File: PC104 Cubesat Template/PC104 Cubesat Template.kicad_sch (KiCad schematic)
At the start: 10 parts

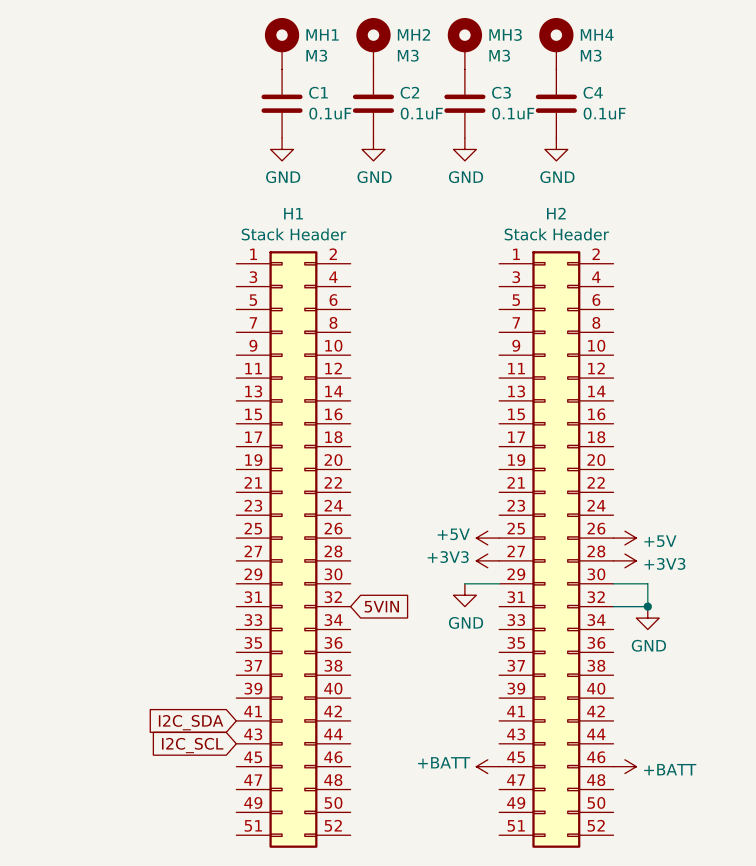
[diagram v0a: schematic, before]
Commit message: add tj bus specific pins
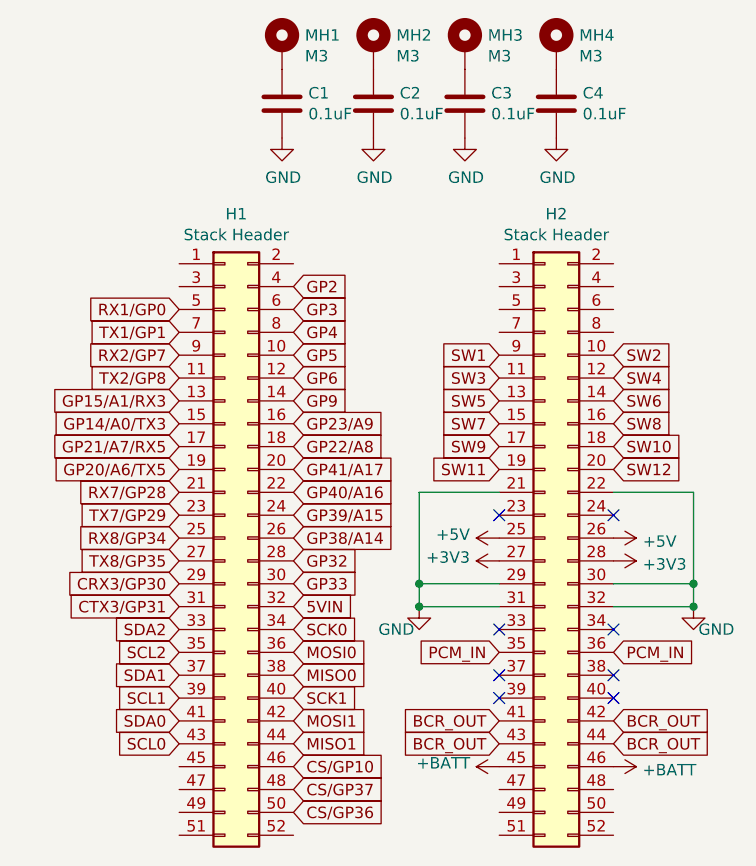
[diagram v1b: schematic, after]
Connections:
- net GND: now also H2.21 (Pin_21), H2.22 (Pin_22), H2.31 (Pin_31)
- net GP5: now reaches H1.10 (Pin_10)
- net TX2/GP8: now reaches H1.11 (Pin_11)
- net GP6: now reaches H1.12 (Pin_12)
- net GP15/A1/RX3: now reaches H1.13 (Pin_13)
- net GP9: now reaches H1.14 (Pin_14)
- net GP14/A0/TX3: now reaches H1.15 (Pin_15)
- net GP23/A9: now reaches H1.16 (Pin_16)
- net GP21/A7/RX5: now reaches H1.17 (Pin_17)
- net GP22/A8: now reaches H1.18 (Pin_18)
- net GP20/A6/TX5: now reaches H1.19 (Pin_19)
- net GP41/A17: now reaches H1.20 (Pin_20)
- net RX7/GP28: now reaches H1.21 (Pin_21)
- net GP40/A16: now reaches H1.22 (Pin_22)
- net TX7/GP29: now reaches H1.23 (Pin_23)
- net GP39/A15: now reaches H1.24 (Pin_24)
- net RX8/GP34: now reaches H1.25 (Pin_25)
- net GP38/A14: now reaches H1.26 (Pin_26)
- net TX8/GP35: now reaches H1.27 (Pin_27)
- net GP32: now reaches H1.28 (Pin_28)
- net CRX3/GP30: now reaches H1.29 (Pin_29)
- net GP33: now reaches H1.30 (Pin_30)
- net CTX3/GP31: now reaches H1.31 (Pin_31)
- net SDA2: now reaches H1.33 (Pin_33)
- net SCK0: now reaches H1.34 (Pin_34)
- net SCL2: now reaches H1.35 (Pin_35)
- net MOSI0: now reaches H1.36 (Pin_36)
- net SDA1: now reaches H1.37 (Pin_37)
- net MISO0: now reaches H1.38 (Pin_38)
- net SCL1: now reaches H1.39 (Pin_39)
- net GP2: now reaches H1.4 (Pin_4)
- net SCK1: now reaches H1.40 (Pin_40)
- net MOSI1: now reaches H1.42 (Pin_42)
- net MISO1: now reaches H1.44 (Pin_44)
- net CS/GP10: now reaches H1.46 (Pin_46)
- net CS/GP37: now reaches H1.48 (Pin_48)
- net RX1/GP0: now reaches H1.5 (Pin_5)
- net CS/GP36: now reaches H1.50 (Pin_50)
- net GP3: now reaches H1.6 (Pin_6)
- net TX1/GP1: now reaches H1.7 (Pin_7)
- net GP4: now reaches H1.8 (Pin_8)
- net RX2/GP7: now reaches H1.9 (Pin_9)
- net SW2: now reaches H2.10 (Pin_10)
- net SW3: now reaches H2.11 (Pin_11)
- net SW4: now reaches H2.12 (Pin_12)
- net SW5: now reaches H2.13 (Pin_13)
- net SW6: now reaches H2.14 (Pin_14)
- net SW7: now reaches H2.15 (Pin_15)
- net SW8: now reaches H2.16 (Pin_16)
- net SW9: now reaches H2.17 (Pin_17)
- net SW10: now reaches H2.18 (Pin_18)
- net SW11: now reaches H2.19 (Pin_19)
- net SW12: now reaches H2.20 (Pin_20)
- net PCM_IN: now reaches H2.35 (Pin_35)
- net PCM_IN: now also H2.36 (Pin_36)
- net BCR_OUT: now reaches H2.41 (Pin_41)
- net BCR_OUT: now also H2.42 (Pin_42), H2.43 (Pin_43), H2.44 (Pin_44)
- net SW1: now reaches H2.9 (Pin_9)
- net I2C_SCL renamed SCL0
- net I2C_SDA renamed SDA0
- no-connect marks 0 -> 8
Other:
- moved on the sheet: H1
